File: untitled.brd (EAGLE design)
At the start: 59.4 x 57.8 mm, 25 parts

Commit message: more clean up, with work based off amatus's designs
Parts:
- 3.3LDO: value LDO1117-33 -> REG1117X; device ldo1117-33:1117-33 -> burr-brown:TO252
- moved 3.3LDO 2.25 mm to (40.3, 24.4)
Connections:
- net +3V3: now also 3.3LDO.3; no longer 3.3LDO.VOUT
- net +5V: now also 3.3LDO.2; no longer 3.3LDO.VIN
- net GND: now also 3.3LDO.1; no longer 3.3LDO.GND
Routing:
- net GND: track 80.1 -> 90.8 mm
- net +3V3: track 289.7 -> 300.3 mm, vias 10 -> 8
- net SCL: track 103.3 -> 107.7 mm, vias 2 -> 1
- net +5V: track 47.5 -> 51.2 mm
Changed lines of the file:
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@@
 <setting verticaltext="up"/>
 </settings>
-<grid distance="0.0125" unitdist="inch" unit="inch" style="lines" multiple="1" display="yes" altdistance="0.025" altunitdist="inch" altunit="inch"/>
+<grid distance="0.0125" unitdist="inch" unit="inch" style="lines" multiple="1" display="no" altdistance="0.025" altunitdist="inch" altunit="inch"/>
 <layers>
 <layer number="1" name="Top" color="4" fill="1" visible="yes" active="yes"/>
@@
 </autorouter>
 <elements>
-<element name="3.3LDO" library="ldo1117-33" package="1117-33" value="LDO1117-33" x="40.64" y="26.67" rot="R180"/>
 <element name="5WAYSWITCH" library="5-wayswitch" package="5-WAYSWITCH" value="5-WAYSWITCH" x="64.77" y="16.51"/>
 <element name="EEPROM" library="adafruit" package="DIL08" value="DS1307" x="85.725" y="59.055" rot="R270"/>
@@
 <element name="C3" library="rcl" package="C0603" value="" x="53.6575" y="51.1175" rot="R90"/>
 <element name="C4" library="SparkFun" package="0603" value="" x="79.6925" y="25.0825" rot="R90"/>
+<element name="3.3LDO" library="burr-brown" package="TO252" value="REG1117X" x="40.3225" y="24.4475" rot="R180"/>
 </elements>
 <signals>
@@
 <wire x1="86.995" y1="27.895" x2="86.995" y2="30.1625" width="0.3048" layer="1"/>
 <via x="86.995" y="30.1625" extent="1-16" drill="0.6" shape="square"/>
-<wire x1="86.995" y1="30.1625" x2="86.995" y2="47.9425" width="0.3048" layer="16"/>
-<wire x1="86.995" y1="47.9425" x2="69.215" y2="65.7225" width="0.3048" layer="16"/>
-<via x="69.215" y="65.7225" extent="1-16" drill="0.6" shape="square"/>
-<wire x1="69.215" y1="65.7225" x2="60.6425" y2="65.7225" width="0.3048" layer="1"/>
-<wire x1="60.6425" y1="65.7225" x2="59.055" y2="67.31" width="0.3048" layer="1"/>
-<wire x1="59.055" y1="67.31" x2="46.99" y2="67.31" width="0.3048" layer="1"/>
+<wire x1="86.995" y1="30.1625" x2="86.995" y2="47.625" width="0.3048" layer="16"/>
 <wire x1="50.8" y1="48.895" x2="53.1825" y2="48.895" width="0.3048" layer="1"/>
 <wire x1="53.1825" y1="48.895" x2="53.5" y2="48.5775" width="0.3048" layer="1" curve="-90"/>
+<wire x1="86.995" y1="47.625" x2="69.215" y2="65.405" width="0.3048" layer="16"/>
+<wire x1="69.215" y1="65.405" x2="61.9125" y2="65.405" width="0.3048" layer="16"/>
+<wire x1="61.9125" y1="65.405" x2="60.0075" y2="67.31" width="0.3048" layer="16"/>
+<wire x1="60.0075" y1="67.31" x2="44.05923125" y2="67.31" width="0.3048" layer="16"/>
+<wire x1="44.05923125" y1="67.31" x2="43.91269375" y2="67.1634625" width="0.3048" layer="16"/>
+<wire x1="43.91269375" y1="67.1634625" x2="43.91269375" y2="66.77269375" width="0.3048" layer="16"/>
+<wire x1="43.91269375" y1="66.77269375" x2="43.18" y2="66.04" width="0.3048" layer="16"/>
 </signal>
 <signal name="SDA">
@@
 <contactref element="EEPROM" pad="2"/>
 <contactref element="GPS" pad="P$8"/>
-<contactref element="3.3LDO" pad="GND"/>
 <contactref element="U$2" pad="25"/>
 <contactref element="U$2" pad="29"/>
@@
 <wire x1="50.5" y1="42.8313" x2="48.2288" y2="42.8313" width="0.4064" layer="1"/>
 <wire x1="48.2288" y1="42.8313" x2="47.625" y2="42.2275" width="0.4064" layer="1"/>
-<wire x1="47.625" y1="42.2275" x2="47.625" y2="41.49" width="0.4064" layer="1"/>
+<wire x1="47.625" y1="42.2275" x2="47.625" y2="41.91" width="0.4064" layer="1"/>
+<wire x1="47.625" y1="41.91" x2="47.625" y2="41.49" width="0.4064" layer="1"/>
 <wire x1="47.625" y1="41.49" x2="47.41" y2="41.275" width="0.4064" layer="1"/>
 <wire x1="50.5" y1="43.4813" x2="48.8788" y2="43.4813" width="0.4064" layer="1"/>
@@
 <via x="60.6425" y="41.5925" extent="1-16" drill="0.6"/>
 <wire x1="55.245" y1="35.56" x2="55.1175" y2="36.3225" width="0.4064" layer="1"/>
-<wire x1="43.18" y1="31.75" x2="43.18" y2="35.56" width="0.4064" layer="1"/>
-<wire x1="43.18" y1="35.56" x2="36.83" y2="41.91" width="0.4064" layer="1"/>
 <wire x1="89.395" y1="27.895" x2="89.395" y2="25.54" width="0.3048" layer="1"/>
 <wire x1="89.395" y1="25.54" x2="89.84" y2="25.095" width="0.3048" layer="1"/>
@@
 <wire x1="53.6575" y1="52.07" x2="53.6575" y2="51.9675" width="0.4064" layer="1"/>
 <wire x1="53.6575" y1="52.07" x2="54.8" y2="52.07" width="0.4064" layer="1"/>
-<wire x1="60.325" y1="59.69" x2="57.785" y2="64.77" width="0" layer="19" extent="1-1"/>
+<contactref element="3.3LDO" pad="1"/>
+<wire x1="42.6025" y1="29.2475" x2="42.6025" y2="41.8525" width="0.4064" layer="1"/>
+<wire x1="36.83" y1="41.91" x2="42.545" y2="41.91" width="0.4064" layer="1"/>
+<wire x1="42.545" y1="41.91" x2="47.625" y2="41.91" width="0.4064" layer="1"/>
+<wire x1="42.6025" y1="41.8525" x2="42.545" y2="41.91" width="0.4064" layer="1" curve="90"/>
 </signal>
 <signal name="+5V">
-<contactref element="3.3LDO" pad="VIN"/>
 <contactref element="LIPOCHARGER-BOOSTER" pad="VCC"/>
 <contactref element="OLED_SCREEN" pad="5V"/>
-<wire x1="38.1" y1="31.75" x2="38.1" y2="38.1" width="0.4064" layer="1"/>
 <wire x1="38.1" y1="38.1" x2="36.83" y2="39.37" width="0.4064" layer="1"/>
 <wire x1="36.83" y1="39.37" x2="39.37" y2="39.6875" width="0.4064" layer="16"/>
 <wire x1="39.37" y1="39.6875" x2="57.4675" y2="58.1025" width="0.4064" layer="16"/>
-<wire x1="57.4675" y1="58.1025" x2="65.7225" y2="58.1025" width="0.4064" layer="16"/>
-<wire x1="65.7225" y1="58.1025" x2="67.945" y2="59.69" width="0.4064" layer="16"/>
+<wire x1="57.4675" y1="58.1025" x2="67.945" y2="58.1025" width="0.4064" layer="16"/>
+<wire x1="67.945" y1="58.1025" x2="67.945" y2="59.69" width="0.4064" layer="16"/>
+<contactref element="3.3LDO" pad="2"/>
+<wire x1="38.0425" y1="29.2475" x2="38.1" y2="29.2475" width="0.4064" layer="1"/>
+<wire x1="38.1" y1="29.2475" x2="38.1" y2="38.1" width="0.4064" layer="1"/>
 </signal>
 <signal name="+3V3">
-<contactref element="3.3LDO" pad="VOUT"/>
 <contactref element="I2C3" pad="2"/>
 <contactref element="I2C4" pad="2"/>
@@
 <wire x1="55.45" y1="38.5313" x2="55.7675" y2="37.475" width="0.4064" layer="1"/>
 <wire x1="54.15" y1="47.1313" x2="54.15" y2="48.1875" width="0.4064" layer="1"/>
-<wire x1="40.64" y1="30.48" x2="40.64" y2="32.385" width="0.4064" layer="1"/>
-<via x="40.64" y="32.385" extent="1-16" drill="0.6"/>
-<wire x1="40.64" y1="32.385" x2="41.5925" y2="32.385" width="0.4064" layer="16"/>
-<wire x1="41.5925" y1="32.385" x2="48.895" y2="39.6875" width="0.4064" layer="16"/>
 <via x="48.895" y="39.6875" extent="1-16" drill="0.6"/>
 <wire x1="48.895" y1="39.6875" x2="48.895" y2="41.06" width="0.4064" layer="1"/>
@@
 <wire x1="77.1525" y1="20.0025" x2="80.3275" y2="20.0025" width="0.3048" layer="1"/>
 <wire x1="80.3275" y1="20.0025" x2="80.3425" y2="18.415" width="0.3048" layer="1"/>
-<wire x1="50.785" y1="15.5575" x2="50.785" y2="36.5275" width="0.3048" layer="1"/>
+<wire x1="50.785" y1="15.5575" x2="50.785" y2="21.9075" width="0.3048" layer="1"/>
+<wire x1="50.785" y1="21.9075" x2="50.785" y2="36.5275" width="0.3048" layer="1"/>
 <wire x1="50.785" y1="36.5275" x2="48.895" y2="38.4175" width="0.3048" layer="1"/>
 <wire x1="48.895" y1="38.4175" x2="48.895" y2="39.6875" width="0.3048" layer="1"/>
@@
 <wire x1="51.435" y1="50.165" x2="51.7525" y2="49.8475" width="0.3048" layer="1"/>
 <wire x1="45.3875" y1="54.61" x2="43.18" y2="54.61" width="0.3048" layer="1"/>
-<via x="43.18" y="54.61" extent="1-16" drill="0.6" shape="square"/>
-<wire x1="43.18" y1="54.61" x2="43.18" y2="45.72" width="0.3048" layer="16"/>
-<wire x1="43.18" y1="45.72" x2="40.9575" y2="43.18" width="0.3048" layer="16"/>
-<wire x1="40.9575" y1="43.18" x2="35.2425" y2="43.18" width="0.3048" layer="16"/>
-<wire x1="35.2425" y1="43.18" x2="35.2425" y2="35.2425" width="0.3048" layer="16"/>
-<wire x1="35.2425" y1="35.2425" x2="37.7825" y2="33.3375" width="0.3048" layer="16"/>
-<wire x1="37.7825" y1="33.3375" x2="39.6875" y2="33.3375" width="0.3048" layer="16"/>
-<wire x1="39.6875" y1="33.3375" x2="40.64" y2="32.385" width="0.3048" layer="16"/>
 <wire x1="43.165" y1="60.96" x2="43.165" y2="54.625" width="0.3048" layer="1"/>
 <wire x1="43.165" y1="54.625" x2="43.18" y2="54.61" width="0.3048" layer="1"/>
@@
 <wire x1="63.1825" y1="22.225" x2="73.65438125" y2="22.225" width="0.3048" layer="16"/>
 <wire x1="73.65438125" y1="22.225" x2="73.6993375" y2="22.26995625" width="0.3048" layer="16"/>
+<contactref element="3.3LDO" pad="3"/>
+<wire x1="40.3225" y1="21.9475" x2="50.785" y2="21.9475" width="0.4064" layer="1"/>
+<wire x1="50.785" y1="21.9475" x2="50.785" y2="21.9075" width="0.4064" layer="1"/>
+<wire x1="43.18" y1="54.61" x2="43.18" y2="43.18" width="0.4064" layer="1"/>
+<wire x1="43.18" y1="43.18" x2="35.2425" y2="43.18" width="0.4064" layer="1"/>
+<wire x1="35.2425" y1="43.18" x2="35.2425" y2="40.64" width="0.4064" layer="1"/>
+<wire x1="35.2425" y1="40.64" x2="40.3225" y2="40.64" width="0.4064" layer="1"/>
+<wire x1="40.3225" y1="40.64" x2="40.3225" y2="21.9475" width="0.4064" layer="1"/>
 </signal>
 </signals>

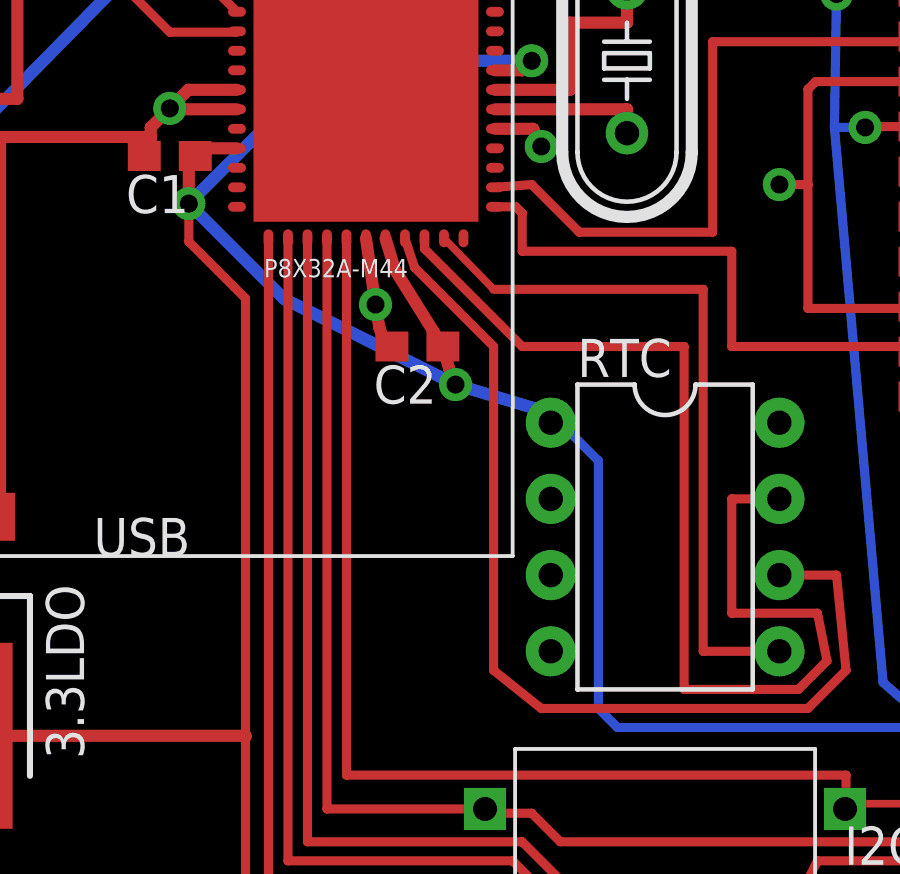
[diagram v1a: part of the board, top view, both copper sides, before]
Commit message: fixed clearance issue
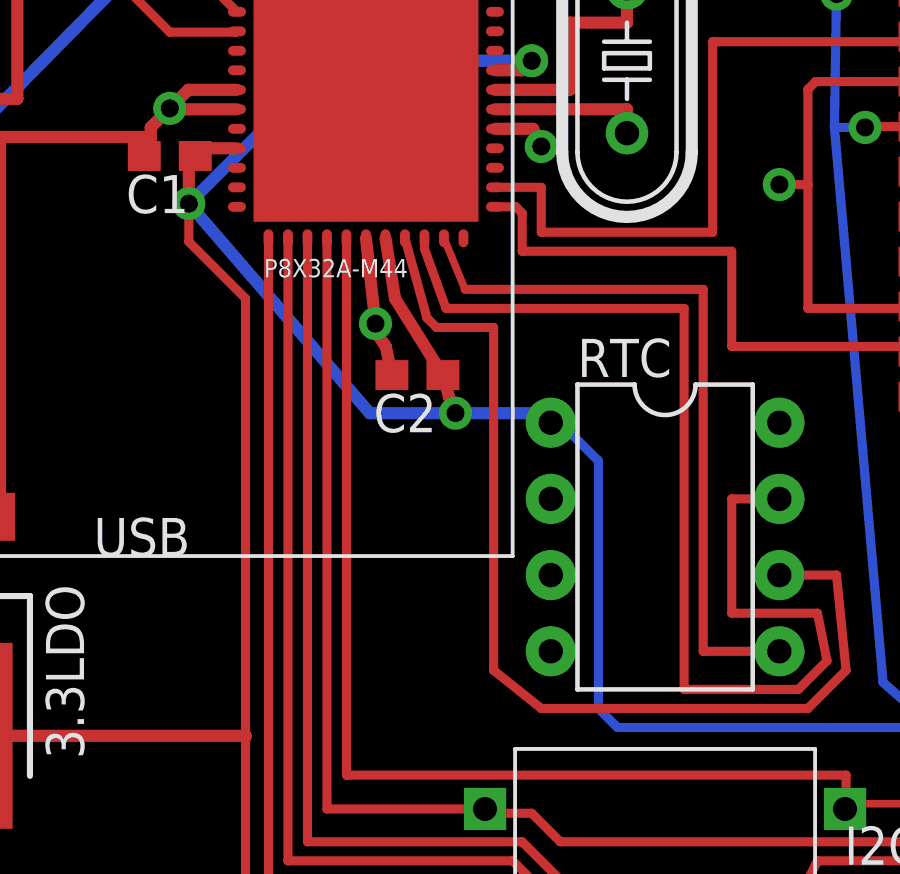
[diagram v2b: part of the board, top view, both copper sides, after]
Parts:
- moved C2 0.95 mm to (56.5, 34.0)
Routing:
- net +3V3: track 300.3 -> 302.3 mm
- net N$8: track 36.8 -> 38.1 mm
- net N$6: track 33.4 -> 34.4 mm
- net N$4: track 22.0 -> 22.9 mm
- net GND: track 90.8 -> 91.6 mm
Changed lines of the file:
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@@
 </classes>
 <designrules name="SparkFun">
-<description language="C">&lt;b&gt;EAGLE Design Rules&lt;/b&gt;
+<description language="en">&lt;b&gt;EAGLE Design Rules&lt;/b&gt;
 &lt;p&gt;
 The default Design Rules have been set to cover
@@
 <element name="U$2" library="SparkFun" package="LCC36" value="HMC6343A" x="86.995" y="23.495"/>
 <element name="C1" library="rcl" package="C0603" value="" x="48.26" y="41.275" rot="R180"/>
-<element name="C2" library="rcl" package="C0603" value="" x="56.515" y="34.925" rot="R180"/>
+<element name="C2" library="rcl" package="C0603" value="" x="56.515" y="33.9725" rot="R180"/>
 <element name="C3" library="rcl" package="C0603" value="" x="53.6575" y="51.1175" rot="R90"/>
 <element name="C4" library="SparkFun" package="0603" value="" x="79.6925" y="25.0825" rot="R90"/>
@@
 <contactref element="RTC" pad="5"/>
 <contactref element="U$1" pad="21"/>
-<wire x1="59.055" y1="36.83" x2="66.04" y2="36.83" width="0.3048" layer="1"/>
+<wire x1="58.1025" y1="36.83" x2="66.04" y2="36.83" width="0.3048" layer="1"/>
 <wire x1="66.04" y1="36.83" x2="66.04" y2="24.765" width="0.3048" layer="1"/>
 <wire x1="66.04" y1="24.765" x2="68.58" y2="24.765" width="0.3048" layer="1"/>
-<wire x1="57.4" y1="38.5313" x2="59.055" y2="36.83" width="0.254" layer="1"/>
+<wire x1="57.4" y1="38.5313" x2="58.1025" y2="36.83" width="0.254" layer="1"/>
 </signal>
 <signal name="N$6">
 <contactref element="RTC" pad="6"/>
 <contactref element="U$1" pad="19"/>
-<wire x1="56.1" y1="38.5313" x2="56.4175" y2="37.5625" width="0.3048" layer="1"/>
-<wire x1="56.4175" y1="37.5625" x2="59.055" y2="34.925" width="0.3048" layer="1"/>
-<wire x1="59.055" y1="34.925" x2="59.055" y2="24.13" width="0.3048" layer="1"/>
+<wire x1="59.055" y1="35.56" x2="59.055" y2="24.13" width="0.3048" layer="1"/>
 <wire x1="59.055" y1="24.13" x2="60.6425" y2="22.86" width="0.3048" layer="1"/>
 <wire x1="60.6425" y1="22.86" x2="69.5325" y2="22.86" width="0.3048" layer="1"/>
@@
 <wire x1="70.8025" y1="24.13" x2="70.485" y2="27.305" width="0.3048" layer="1"/>
 <wire x1="70.485" y1="27.305" x2="68.58" y2="27.305" width="0.3048" layer="1"/>
+<wire x1="56.1" y1="38.5313" x2="56.8325" y2="35.8775" width="0.3048" layer="1"/>
+<wire x1="56.8325" y1="35.8775" x2="57.15" y2="35.56" width="0.3048" layer="1"/>
+<wire x1="57.15" y1="35.56" x2="59.055" y2="35.56" width="0.3048" layer="1"/>
 </signal>
 <signal name="N$8">
 <contactref element="RTC" pad="7"/>
 <contactref element="U$1" pad="20"/>
-<wire x1="60.0075" y1="34.925" x2="65.405" y2="34.925" width="0.3048" layer="1"/>
-<wire x1="65.405" y1="34.925" x2="65.405" y2="23.495" width="0.3048" layer="1"/>
+<wire x1="57.4675" y1="36.195" x2="65.405" y2="36.195" width="0.3048" layer="1"/>
+<wire x1="65.405" y1="36.195" x2="65.405" y2="23.495" width="0.3048" layer="1"/>
 <wire x1="65.405" y1="23.495" x2="69.215" y2="23.495" width="0.3048" layer="1"/>
 <wire x1="69.215" y1="23.495" x2="70.1675" y2="24.4475" width="0.3048" layer="1"/>
@@
 <wire x1="66.9925" y1="29.845" x2="68.58" y2="29.845" width="0.3048" layer="1"/>
 <wire x1="56.75" y1="38.5313" x2="56.75" y2="38.1825" width="0.3048" layer="1"/>
-<wire x1="56.75" y1="38.1825" x2="60.0075" y2="34.925" width="0.3048" layer="1"/>
+<wire x1="56.75" y1="38.1825" x2="57.4675" y2="36.195" width="0.3048" layer="1"/>
 </signal>
 <signal name="SCL">
@@
 <contactref element="GPS" pad="P$2"/>
 <wire x1="66.3575" y1="45.085" x2="66.3575" y2="38.735" width="0.3048" layer="1"/>
-<wire x1="66.3575" y1="38.735" x2="61.9125" y2="38.735" width="0.3048" layer="1"/>
-<wire x1="61.9125" y1="38.735" x2="60.325" y2="40.3225" width="0.3048" layer="1"/>
-<wire x1="60.325" y1="40.3225" x2="59.1" y2="40.2313" width="0.3048" layer="1"/>
+<wire x1="66.3575" y1="38.735" x2="60.6425" y2="38.735" width="0.3048" layer="1"/>
 <wire x1="74.05" y1="45.255" x2="73.88" y2="45.085" width="0.3048" layer="1"/>
 <wire x1="73.88" y1="45.085" x2="66.3575" y2="45.085" width="0.3048" layer="1"/>
+<wire x1="59.1" y1="40.2313" x2="60.6425" y2="40.2313" width="0.3048" layer="1"/>
+<wire x1="60.6425" y1="40.2313" x2="60.6425" y2="38.735" width="0.3048" layer="1"/>
 </signal>
 <signal name="N$7">
@@
 <vertex x="33.655" y="10.16"/>
 </polygon>
-<wire x1="54.8" y1="38.5313" x2="55.1175" y2="36.3225" width="0.4064" layer="1"/>
-<wire x1="55.245" y1="35.56" x2="55.46" y2="34.925" width="0.4064" layer="1"/>
-<wire x1="55.46" y1="34.925" x2="55.665" y2="34.925" width="0.4064" layer="1"/>
+<wire x1="54.8" y1="38.5313" x2="55.1175" y2="35.6875" width="0.4064" layer="1"/>
+<wire x1="55.245" y1="35.2425" x2="55.46" y2="34.925" width="0.4064" layer="1"/>
+<wire x1="55.46" y1="34.925" x2="55.665" y2="33.9725" width="0.4064" layer="1"/>
 <wire x1="54.8" y1="47.1313" x2="54.8" y2="52.07" width="0.4064" layer="1"/>
 <wire x1="54.8" y1="52.07" x2="54.4825" y2="53.4675" width="0.4064" layer="1"/>
@@
 <via x="48.26" y="42.8625" extent="1-16" drill="0.6"/>
 <via x="54.4825" y="53.4675" extent="1-16" drill="0.6"/>
-<via x="55.1175" y="36.3225" extent="1-16" drill="0.6"/>
+<via x="55.1175" y="35.6875" extent="1-16" drill="0.6"/>
 <wire x1="59.1" y1="42.1813" x2="60.3712" y2="42.1813" width="0.4064" layer="1"/>
 <wire x1="60.3712" y1="42.1813" x2="60.6425" y2="41.5925" width="0.4064" layer="1"/>
 <via x="60.6425" y="41.5925" extent="1-16" drill="0.6"/>
-<wire x1="55.245" y1="35.56" x2="55.1175" y2="36.3225" width="0.4064" layer="1"/>
+<wire x1="55.245" y1="35.2425" x2="55.1175" y2="35.6875" width="0.4064" layer="1"/>
 <wire x1="89.395" y1="27.895" x2="89.395" y2="25.54" width="0.3048" layer="1"/>
 <wire x1="89.395" y1="25.54" x2="89.84" y2="25.095" width="0.3048" layer="1"/>
@@
 <wire x1="50.5" y1="41.5313" x2="49.11" y2="41.5313" width="0.4064" layer="1"/>
 <wire x1="49.11" y1="41.5313" x2="49.11" y2="41.275" width="0.4064" layer="1"/>
-<wire x1="55.45" y1="38.5313" x2="55.7675" y2="37.475" width="0.4064" layer="1"/>
 <wire x1="54.15" y1="47.1313" x2="54.15" y2="48.1875" width="0.4064" layer="1"/>
 <via x="48.895" y="39.6875" extent="1-16" drill="0.6"/>
 <wire x1="48.895" y1="39.6875" x2="48.895" y2="41.06" width="0.4064" layer="1"/>
 <wire x1="48.895" y1="41.06" x2="49.11" y2="41.275" width="0.4064" layer="1"/>
-<wire x1="57.365" y1="34.925" x2="57.57" y2="34.1875" width="0.4064" layer="1"/>
-<wire x1="57.57" y1="34.1875" x2="57.785" y2="33.655" width="0.4064" layer="1"/>
-<via x="57.785" y="33.655" extent="1-16" drill="0.6"/>
-<wire x1="57.785" y1="33.655" x2="52.07" y2="36.5125" width="0.4064" layer="16"/>
-<wire x1="52.07" y1="36.5125" x2="48.895" y2="39.6875" width="0.4064" layer="16"/>
+<wire x1="57.365" y1="33.9725" x2="57.57" y2="33.235" width="0.4064" layer="1"/>
+<wire x1="57.57" y1="33.235" x2="57.785" y2="32.7025" width="0.4064" layer="1"/>
+<via x="57.785" y="32.7025" extent="1-16" drill="0.6"/>
+<wire x1="57.785" y1="32.7025" x2="54.9275" y2="32.7025" width="0.4064" layer="16"/>
+<wire x1="54.9275" y1="32.7025" x2="48.895" y2="39.6875" width="0.4064" layer="16"/>
 <wire x1="59.1" y1="44.1313" x2="60.0063" y2="44.1313" width="0.4064" layer="1"/>
 <wire x1="60.0063" y1="44.1313" x2="60.325" y2="44.45" width="0.4064" layer="1"/>
@@
 <wire x1="51.7525" y1="49.8475" x2="52.3875" y2="45.72" width="0.4064" layer="16"/>
 <wire x1="52.3875" y1="45.72" x2="53.6575" y2="44.45" width="0.4064" layer="16"/>
-<wire x1="55.7675" y1="37.475" x2="57.365" y2="34.925" width="0.4064" layer="1"/>
+<wire x1="55.7675" y1="36.5225" x2="57.365" y2="33.9725" width="0.4064" layer="1"/>
 <wire x1="60.96" y1="32.385" x2="60.96" y2="32.7025" width="0.4064" layer="16"/>
-<wire x1="60.96" y1="32.7025" x2="57.785" y2="33.655" width="0.4064" layer="16"/>
+<wire x1="60.96" y1="32.7025" x2="57.785" y2="32.7025" width="0.4064" layer="16"/>
 <wire x1="72.035975" y1="23.725396875" x2="73.6993375" y2="22.26995625" width="0.3048" layer="16"/>
 <wire x1="73.6993375" y1="22.26995625" x2="75.565" y2="20.6375" width="0.3048" layer="16"/>
@@
 <wire x1="35.2425" y1="40.64" x2="40.3225" y2="40.64" width="0.4064" layer="1"/>
 <wire x1="40.3225" y1="40.64" x2="40.3225" y2="21.9475" width="0.4064" layer="1"/>
+<wire x1="55.45" y1="38.5313" x2="55.7675" y2="36.5225" width="0.4064" layer="1"/>
 </signal>
 </signals>
